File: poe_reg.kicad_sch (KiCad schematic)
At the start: 21 parts, among them U3 MP6004GQ-P

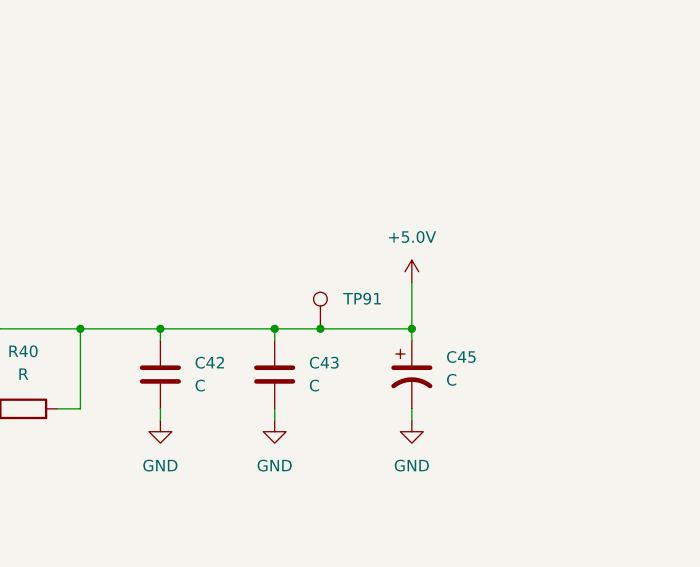
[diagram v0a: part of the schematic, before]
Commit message: did 3v3 reg
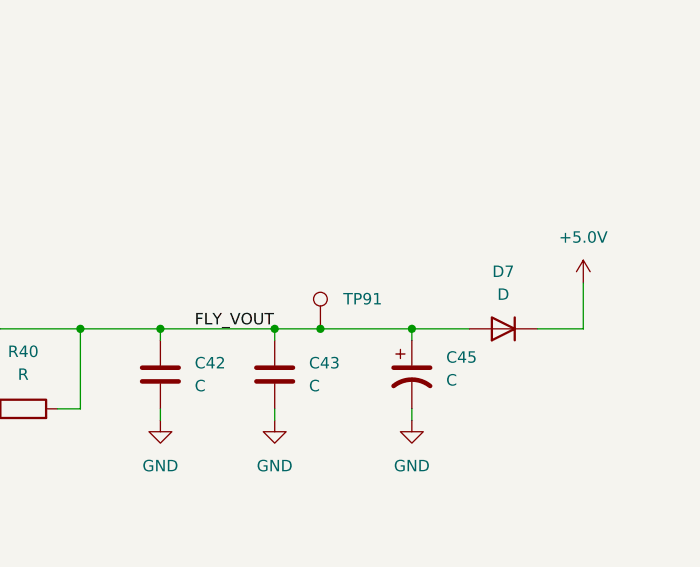
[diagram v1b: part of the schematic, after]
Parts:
- added D7: D, symbol Device:D
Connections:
- net +5.0V: now also D7.1 (K); no longer C42.1, C43.1, C45.1, D6.1 (K), R40.2, TP91.1
- new net FLY_VOUT: C42.1, C43.1, C45.1, D6.1 (K), D7.2 (A), R40.2, TP91.1
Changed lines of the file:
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@@
+	)
+	(junction
+		(at 250.19 88.9)
+		(diameter 0)
+		(color 0 0 0 0)
 	)
 	(junction
@@
 	)
 	(junction
-		(at 250.19 88.9)
-		(diameter 0)
-		(color 0 0 0 0)
-	)
-	(junction
 		(at 139.7 67.31)
 		(diameter 0)
@@
 	(wire
 		(pts
+			(xy 264.16 88.9) (xy 269.24 88.9)
+		)
+		(stroke
+			(width 0)
+			(type default)
+		)
+	)
+	(wire
+		(pts
 			(xy 149.86 77.47) (xy 139.7 77.47)
 		)
@@
 	(wire
 		(pts
-			(xy 250.19 83.82) (xy 250.19 88.9)
-		)
-		(stroke
-			(width 0)
-			(type default)
-		)
-	)
-	(wire
-		(pts
 			(xy 149.86 77.47) (xy 149.86 78.74)
 		)
@@
 	(wire
 		(pts
+			(xy 250.19 88.9) (xy 256.54 88.9)
+		)
+		(stroke
+			(width 0)
+			(type default)
+		)
+	)
+	(wire
+		(pts
 			(xy 250.19 97.79) (xy 250.19 99.06)
 		)
@@
 		(pts
 			(xy 86.36 92.71) (xy 92.71 92.71)
+		)
+		(stroke
+			(width 0)
+			(type default)
+		)
+	)
+	(wire
+		(pts
+			(xy 269.24 83.82) (xy 269.24 88.9)
 		)
 		(stroke
@@
 	(label "FLY_SW"
 		(at 135.89 93.98 0)
+		(effects
+			(font
+				(size 1.27 1.27)
+			)
+			(justify left bottom)
+		)
+	)
+	(label "FLY_VOUT"
+		(at 226.06 88.9 0)
 		(effects
 			(font
@@
 	)
 	(symbol
+		(lib_id "Device:D")
+		(at 260.35 88.9 180)
+		(unit 1)
+		(exclude_from_sim no)
+		(in_bom yes)
+		(on_board yes)
+		(dnp no)
+		(fields_autoplaced yes)
+		(property "Reference" "D7"
+			(at 260.35 82.55 0)
+			(effects
+				(font
+					(size 1.27 1.27)
+				)
+			)
+		)
+		(property "Value" "D"
+			(at 260.35 85.09 0)
+			(effects
+				(font
+					(size 1.27 1.27)
+				)
+			)
+		)
+		(property "Footprint" ""
+			(at 260.35 88.9 0)
+			(effects
+				(font
+					(size 1.27 1.27)
+				)
+				(hide yes)
+			)
+		)
+		(property "Datasheet" "~"
+			(at 260.35 88.9 0)
+			(effects
+				(font
+					(size 1.27 1.27)
+				)
+				(hide yes)
+			)
+		)
+		(property "Description" "Diode"
+			(at 260.35 88.9 0)
+			(effects
+				(font
+					(size 1.27 1.27)
+				)
+				(hide yes)
+			)
+		)
+		(property "Sim.Device" "D"
+			(at 260.35 88.9 0)
+			(effects
+				(font
+					(size 1.27 1.27)
+				)
+				(hide yes)
+			)
+		)
+		(property "Sim.Pins" "1=K 2=A"
+			(at 260.35 88.9 0)
+			(effects
+				(font
+					(size 1.27 1.27)
+				)
+				(hide yes)
+			)
+		)
+		(pin "2"
+		)
+		(pin "1"
+		)
+		(instances
+			(project ""
+				(path "/2970f661-65ab-4e2b-aeda-d76d1044f2b8/475d46f3-a9d1-4d0e-882c-449f9a11ef3e"
+					(reference "D7")
+					(unit 1)
+				)
+			)
+		)
+	)
+	(symbol
 		(lib_id "Connector:TestPoint_Alt")
 		(at 154.94 135.89 0)
@@
 	(symbol
 		(lib_id "power:+3.3V")
-		(at 250.19 83.82 0)
+		(at 269.24 83.82 0)
 		(unit 1)
 		(exclude_from_sim no)
@@
 		(fields_autoplaced yes)
 		(property "Reference" "#PWR074"
-			(at 250.19 87.63 0)
+			(at 269.24 87.63 0)
 			(effects
 				(font
@@
 		)
 		(property "Value" "+5.0V"
-			(at 250.19 78.74 0)
+			(at 269.24 78.74 0)
 			(effects
 				(font
@@
 		)
 		(property "Footprint" ""
-			(at 250.19 83.82 0)
+			(at 269.24 83.82 0)
 			(effects
 				(font
@@
 		)
 		(property "Datasheet" ""
-			(at 250.19 83.82 0)
+			(at 269.24 83.82 0)
 			(effects
 				(font
@@
 		)
 		(property "Description" "Power symbol creates a global label with name \"+3.3V\""
-			(at 250.19 83.82 0)
-			(effects
-				(font
-					(size 1.27 1.27)
-				)
-				(hide yes)
-			)
-		)
-		(pin "1"
-		)
-		(instances
-			(project ""
+			(at 269.24 83.82 0)
+			(effects
+				(font
+					(size 1.27 1.27)
+				)
+				(hide yes)
+			)
+		)
+		(pin "1"
+		)
+		(instances
+			(project "netdaq"
 				(path "/2970f661-65ab-4e2b-aeda-d76d1044f2b8/475d46f3-a9d1-4d0e-882c-449f9a11ef3e"
 					(reference "#PWR074")

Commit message: did stuff
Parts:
- renumbered C38 to C102, C42 to C103, C43 to C104, C45 to C105, C40 to C106, C39 to C107, C41 to C108, D5 to D37, D6 to D38, D7 to D39, R37 to R76, R40 to R77, R38 to R78, R39 to R79, TP93 to TP122, TP90 to TP123, TP91 to TP124, TP92 to TP125, TP94 to TP126, TP95 to TP127, U3 to U5

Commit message: lots
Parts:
- removed D39: D, symbol Device:D
- removed TR2: Wuerth_750343373, Transformer_THT:Transformer_Wuerth_750343373, symbol Transformer:Wuerth_750343373
- added C134: 47u, Capacitor_SMD:C_Elec_10x10.2, symbol Device:C_Polarized_US
- added D80: MMBZ5256ELT1G, MMBZ5256ELT1G:SOT-23(1-3), symbol Device:D_Zener
- added R103: 500, Resistor_SMD:R_0603_1608Metric, symbol Device:R
- added R104: 13k, Resistor_SMD:R_0402_1005Metric, symbol Device:R
- added R105: 10k, Resistor_SMD:R_0402_1005Metric, symbol Device:R
- added R106: 330k, Resistor_SMD:R_0402_1005Metric, symbol Device:R
- added T2: POE30P-50L, POE30P-50L:POE30P-50L, symbol POE30P-50L:POE30P-50L
- C102: value C -> 910p; footprint (none) -> Capacitor_SMD:C_0402_1005Metric
- C103, C104: value C -> 22u 10 V; footprint (none) -> Capacitor_SMD:C_0805_2012Metric
- C105: value C -> 220u; footprint (none) -> Capacitor_SMD:C_Elec_6.3x7.7
- C106: value C -> 2.2u 100 V; footprint (none) -> Capacitor_SMD:C_1206_3216Metric
- C107: value C -> 1u 10V; footprint (none) -> Capacitor_SMD:C_0402_1005Metric
- C108: footprint (none) -> Capacitor_SMD:C_0402_1005Metric; now not fitted
- D37: value D -> US1MFA; footprint (none) -> Diode_SMD:D_SOD-123F
- D38: value D -> VS-10BQ060-M3/5BT; footprint (none) -> SMB:SMB(DO-214AA); symbol Device:D -> Device:D_Schottky
- R76: value R -> 56k; footprint (none) -> Resistor_SMD:R_0402_1005Metric
- R77: footprint (none) -> Resistor_SMD:R_0402_1005Metric; now not fitted
- R78: value R -> 68k; footprint (none) -> Resistor_SMD:R_0402_1005Metric
- R79: value R -> 12k; footprint (none) -> Resistor_SMD:R_0402_1005Metric
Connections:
- net ETH_SHIELD is gone; now on net PGND: C106.2, C107.2, R79.2, TP126.1, U5.1 (GND), U5.10 (AGND), U5.15 (EPAD), U5.2 (GND)
- net FLY_VOUT is gone; now on net +5.0V: C103.1, C104.1, C105.1, D38.1 (K), R77.2, TP124.1
- net +5.0V: now also R103.2
- net FLY_CT: now also T2.2
- net FLY_SW: now also T2.3
- net GND: now also R103.1, T2.7, T2.8
- net VIN: now also C134.1, D80.1 (K), T2.4
- net at C108.1, D38.2 (A), TP123.1: now also T2.5, T2.6
- net FLY_EN: now reaches U5.3 (EN)
- net FLY_EN: now also R104.1, R105.2
- net PGND: now reaches U5.7 (MODE)
- net PGND: now also C134.2, R104.2, R106.2, T2.1
- net at U5.9 (ILIM): now also R106.1
- new net: D80.2 (A), R105.1
- no-connect marks 0 -> 1
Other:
- moved on the sheet: C102, C103, C104, C105, C107, D37, D38, R76, R78, R79, TP122, TP123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

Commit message: changed to 4 layer, finished usb conn, added jtag conn, some other things
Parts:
- TP122, TP123, TP124, TP125: footprint (none) -> TestPoint:TestPoint_THTPad_D1.0mm_Drill0.5mm
- TP126, TP127: footprint (none) -> TestPoint:TestPoint_THTPad_1.0x1.0mm_Drill0.5mm
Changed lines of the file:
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@@
 			)
 		)
-		(property "Footprint" ""
+		(property "Footprint" "TestPoint:TestPoint_THTPad_D1.0mm_Drill0.5mm"
 			(at 228.6 124.46 0)
 			(hide yes)
@@
 			)
 		)
-		(property "Footprint" ""
+		(property "Footprint" "TestPoint:TestPoint_THTPad_1.0x1.0mm_Drill0.5mm"
 			(at 198.12 207.01 0)
 			(hide yes)
@@
 			)
 		)
-		(property "Footprint" ""
+		(property "Footprint" "TestPoint:TestPoint_THTPad_D1.0mm_Drill0.5mm"
 			(at 191.77 109.22 0)
 			(hide yes)
@@
 			)
 		)
-		(property "Footprint" ""
+		(property "Footprint" "TestPoint:TestPoint_THTPad_D1.0mm_Drill0.5mm"
 			(at 191.77 135.89 0)
 			(hide yes)
@@
 			)
 		)
-		(property "Footprint" ""
+		(property "Footprint" "TestPoint:TestPoint_THTPad_D1.0mm_Drill0.5mm"
 			(at 283.21 124.46 0)
 			(hide yes)
@@
 			)
 		)
-		(property "Footprint" ""
+		(property "Footprint" "TestPoint:TestPoint_THTPad_1.0x1.0mm_Drill0.5mm"
 			(at 232.41 177.8 0)
 			(hide yes)

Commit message: many stuffs
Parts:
- added TP180: TestPoint, TestPoint:TestPoint_THTPad_D1.0mm_Drill0.5mm, symbol Connector:TestPoint
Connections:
- net FLY_EN: now also TP180.1
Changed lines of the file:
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@@
+	)
+	(junction
+		(at 105.41 149.86)
+		(diameter 0)
+		(color 0 0 0 0)
 	)
 	(junction
@@
 	(wire
 		(pts
+			(xy 105.41 148.59) (xy 105.41 149.86)
+		)
+		(stroke
+			(width 0)
+			(type default)
+		)
+	)
+	(wire
+		(pts
 			(xy 109.22 109.22) (xy 124.46 109.22)
 		)
@@
 	(wire
 		(pts
-			(xy 96.52 149.86) (xy 133.35 149.86)
+			(xy 96.52 149.86) (xy 105.41 149.86)
 		)
 		(stroke
@@
 		(pts
 			(xy 118.11 143.51) (xy 118.11 144.78)
+		)
+		(stroke
+			(width 0)
+			(type default)
+		)
+	)
+	(wire
+		(pts
+			(xy 105.41 149.86) (xy 133.35 149.86)
 		)
 		(stroke
@@
 					(unit 1)
 				)
+			)
+		)
+	)
+	(symbol
+		(lib_id "Connector:TestPoint")
+		(at 105.41 148.59 0)
+		(mirror y)
+		(unit 1)
+		(body_style 1)
+		(exclude_from_sim no)
+		(in_bom yes)
+		(on_board yes)
+		(in_pos_files yes)
+		(dnp no)
+		(fields_autoplaced yes)
+		(property "Reference" "TP180"
+			(at 107.95 145.2879 0)
+			(show_name no)
+			(do_not_autoplace no)
+			(effects
+				(font
+					(size 1.27 1.27)
+				)
+				(justify right)
+			)
+		)
+		(property "Value" "TestPoint"
+			(at 104.1401 143.51 90)
+			(hide yes)
+			(show_name no)
+			(do_not_autoplace no)
+			(effects
+				(font
+					(size 1.27 1.27)
+				)
+				(justify left)
+			)
+		)
+		(property "Footprint" "TestPoint:TestPoint_THTPad_D1.0mm_Drill0.5mm"
+			(at 100.33 148.59 0)
+			(hide yes)
+			(show_name no)
+			(do_not_autoplace no)
+			(effects
+				(font
+					(size 1.27 1.27)
+				)
+			)
+		)
+		(property "Datasheet" ""
+			(at 100.33 148.59 0)
+			(hide yes)
+			(show_name no)
+			(do_not_autoplace no)
+			(effects
+				(font
+					(size 1.27 1.27)
+				)
+			)
+		)
+		(property "Description" "test point"
+			(at 105.41 148.59 0)
+			(hide yes)
+			(show_name no)
+			(do_not_autoplace no)
+			(effects
+				(font
+					(size 1.27 1.27)
+				)
+			)
+		)
+		(pin "1"
+		)
+		(instances
+			(project "netdaq"
+				(path "/2970f661-65ab-4e2b-aeda-d76d1044f2b8/475d46f3-a9d1-4d0e-882c-449f9a11ef3e"
+					(reference "TP180")
+					(unit 1)
+				)

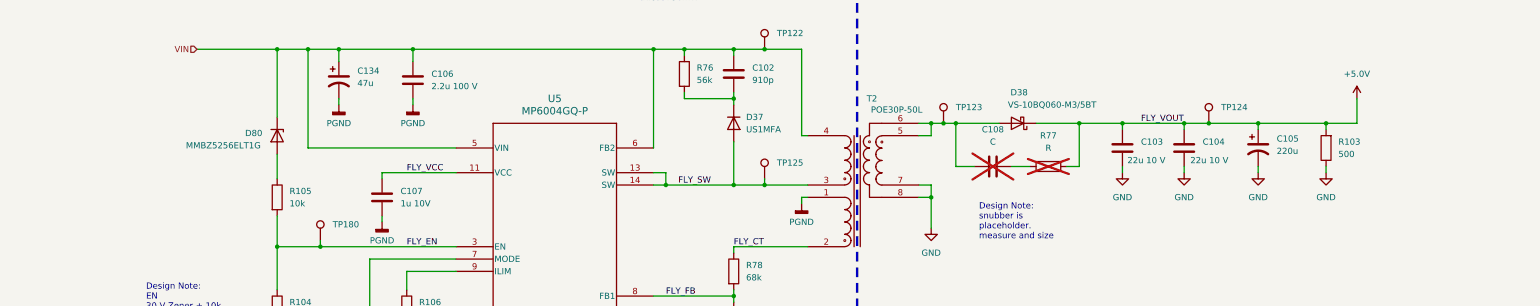
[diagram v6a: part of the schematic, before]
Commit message: did a bunch of bom matching to lcsc
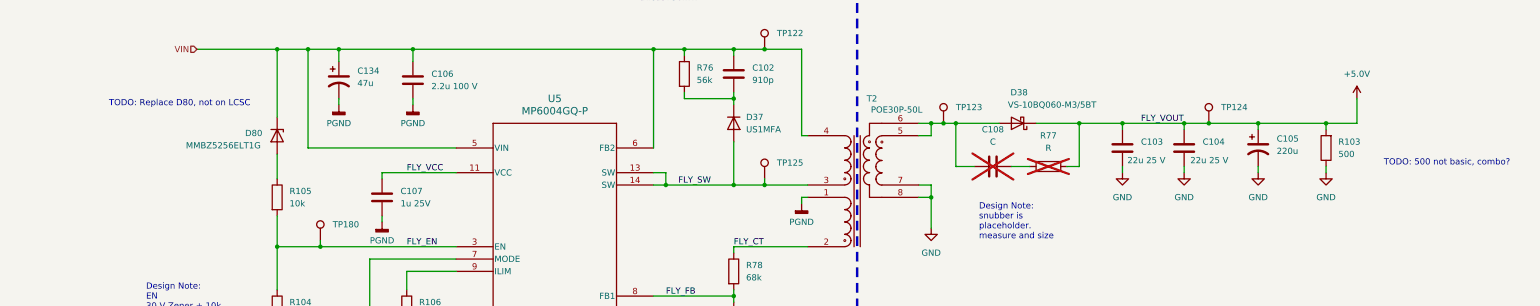
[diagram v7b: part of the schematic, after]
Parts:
- C102, C105, C134, R103: LCSC Basic/Pref (none) -> n
- C103, C104: value 22u 10 V -> 22u 25 V; LCSC (none) -> C45783; LCSC Basic/Pref (none) -> x; LCSC Part (none) -> C45783
- C107: value 1u 10V -> 1u 25V; LCSC (none) -> C52923; LCSC Basic/Pref (none) -> x; LCSC Part (none) -> C52923
- D37: LCSC Part (none) -> C894760
- D38: LCSC (none) -> C469520; LCSC Part (none) -> C469520
- D80, T2, U5: LCSC missing (none) -> x
- R104: footprint Resistor_SMD:R_0402_1005Metric -> Resistor_SMD:R_0603_1608Metric; LCSC (none) -> C22797; LCSC Basic/Pref (none) -> x; LCSC Part (none) -> C22797
- R105: LCSC (none) -> C25744; LCSC Basic/Pref (none) -> x; LCSC Part (none) -> C25744
- R106: LCSC (none) -> C25778; LCSC Basic/Pref (none) -> x; LCSC Part (none) -> C25778
- R76: LCSC (none) -> C25796; LCSC Basic/Pref (none) -> x; LCSC Part (none) -> C25796
- R78: LCSC (none) -> C36871; LCSC Basic/Pref (none) -> x; LCSC Part (none) -> C36871
- R79: LCSC (none) -> C25752; LCSC Basic/Pref (none) -> x; LCSC Part (none) -> C25752
- TP122, TP123, TP124, TP125, TP126, TP127, TP180: now left out of the parts list
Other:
- note added: "TODO: 500 not basic, combo?"
- note added: "TODO: Replace D80, not on LCSC"

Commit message: did almost nothing!
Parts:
- added R107: 200, Resistor_SMD:R_0603_1608Metric, symbol Device:R
- R103: value 500 -> 300; LCSC (none) -> C25102; LCSC Basic/Pref n -> y; LCSC Part (none) -> C25102
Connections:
- net GND: now also R107.1; no longer R103.1
- net +5.0V renamed +5.2V
- new net: R103.1, R107.2
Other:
- note added: "TODO: recalc for 5.2 V"
- note removed: "TODO: 500 not basic, combo?"
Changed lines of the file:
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@@
 	(generator_version "10.0")
 	(paper "A3")
-	(text "TODO: 500 not basic, combo?"
+	(text "TODO: recalc for 5.2 V"
 		(exclude_from_sim no)
-		(at 337.312 132.588 0)
+		(at 133.858 98.806 0)
 		(effects
 			(font
@@
 	(wire
 		(pts
+			(xy 312.42 133.35) (xy 312.42 135.89)
+		)
+		(stroke
+			(width 0)
+			(type default)
+		)
+	)
+	(wire
+		(pts
 			(xy 132.08 180.34) (xy 133.35 180.34)
 		)
@@
 	(wire
 		(pts
+			(xy 312.42 143.51) (xy 312.42 146.05)
+		)
+		(stroke
+			(width 0)
+			(type default)
+		)
+	)
+	(wire
+		(pts
 			(xy 173.99 134.62) (xy 176.53 134.62)
 		)
@@
 	(wire
 		(pts
-			(xy 312.42 133.35) (xy 312.42 134.62)
-		)
-		(stroke
-			(width 0)
-			(type default)
-		)
-	)
-	(wire
-		(pts
 			(xy 228.6 127) (xy 231.14 127)
 		)
@@
 	)
 	(symbol
+		(lib_id "Device:R")
+		(at 312.42 139.7 180)
+		(unit 1)
+		(body_style 1)
+		(exclude_from_sim no)
+		(in_bom yes)
+		(on_board yes)
+		(in_pos_files yes)
+		(dnp no)
+		(fields_autoplaced yes)
+		(property "Reference" "R107"
+			(at 314.96 138.4299 0)
+			(show_name no)
+			(do_not_autoplace no)
+			(effects
+				(font
+					(size 1.27 1.27)
+				)
+				(justify right)
+			)
+		)
+		(property "Value" "200"
+			(at 314.96 140.9699 0)
+			(show_name no)
+			(do_not_autoplace no)
+			(effects
+				(font
+					(size 1.27 1.27)
+				)
+				(justify right)
+			)
+		)
+		(property "Footprint" "Resistor_SMD:R_0603_1608Metric"
+			(at 314.198 139.7 90)
+			(hide yes)
+			(show_name no)
+			(do_not_autoplace no)
+			(effects
+				(font
+					(size 1.27 1.27)
+				)
+			)
+		)
+		(property "Datasheet" ""
+			(at 312.42 139.7 0)
+			(hide yes)
+			(show_name no)
+			(do_not_autoplace no)
+			(effects
+				(font
+					(size 1.27 1.27)
+				)
+			)
+		)
+		(property "Description" "Resistor"
+			(at 312.42 139.7 0)
+			(hide yes)
+			(show_name no)
+			(do_not_autoplace no)
+			(effects
+				(font
+					(size 1.27 1.27)
+				)
+			)
+		)
+		(property "Sim.Type" ""
+			(at 312.42 139.7 0)
+			(hide yes)
+			(show_name no)
+			(do_not_autoplace no)
+			(effects
+				(font
+					(size 1.27 1.27)
+				)
+			)
+		)
+		(property "KLC_S3.3" ""
+			(at 312.42 139.7 0)
+			(hide yes)
+			(show_name no)
+			(do_not_autoplace no)
+			(effects
+				(font
+					(size 1.27 1.27)
+				)
+			)
+		)
+		(property "KLC_S4.1" ""
+			(at 312.42 139.7 0)
+			(hide yes)
+			(show_name no)
+			(do_not_autoplace no)
+			(effects
+				(font
+					(size 1.27 1.27)
+				)
+			)
+		)
+		(property "LCSC Basic/Pref" "y"
+			(at 312.42 139.7 0)
+			(hide yes)
+			(show_name no)
+			(do_not_autoplace no)
+			(effects
+				(font
+					(size 1.27 1.27)
+				)
+			)
+		)
+		(property "LCSC missing" ""
+			(at 312.42 139.7 0)
+			(hide yes)
+			(show_name no)
+			(do_not_autoplace no)
+			(effects
+				(font
+					(size 1.27 1.27)
+				)
+			)
+		)
+		(property "LCSC" "C25087"
+			(at 312.42 139.7 0)
+			(hide yes)
+			(show_name no)
+			(do_not_autoplace no)
+			(effects
+				(font
+					(size 1.27 1.27)
+				)
+			)
+		)
+		(property "LCSC Part" "C25087"
+			(at 312.42 139.7 0)
+			(hide yes)
+			(show_name no)
+			(do_not_autoplace no)
+			(effects
+				(font
+					(size 1.27 1.27)
+				)
+			)
+		)
+		(pin "1"
+		)
+		(pin "2"
+		)
+		(instances
+			(project "netdaq"
+				(path "/2970f661-65ab-4e2b-aeda-d76d1044f2b8/475d46f3-a9d1-4d0e-882c-449f9a11ef3e"
+					(reference "R107")
+					(unit 1)
+				)
+			)
+		)
+	)
+	(symbol
 		(lib_id "Device:D_Schottky")
 		(at 248.92 124.46 180)
@@
 			)
 		)
-		(property "Value" "500"
+		(property "Value" "300"
 			(at 314.96 130.8099 0)
 			(show_name no)
@@
 			)
 		)
-		(property "LCSC Basic/Pref" "n"
+		(property "LCSC Basic/Pref" "y"
 			(at 312.42 129.54 0)
 			(hide yes)
@@
 			)
 		)
-		(pin "1"
-		)
-		(pin "2"
-		)
-		(instances
-			(project "netdaq"
-				(path "/2970f661-65ab-4e2b-aeda-d76d1044f2b8/475d46f3-a9d1-4d0e-882c-449f9a11ef3e"
-					(reference "R103")
-					(unit 1)
-				)
-			)
-		)
-	)
-	(symbol
-		(lib_id "power:GND")
-		(at 312.42 134.62 0)
-		(unit 1)
-		(body_style 1)
-		(exclude_from_sim no)
-		(in_bom yes)
-		(on_board yes)
-		(in_pos_files yes)
-		(dnp no)
-		(fields_autoplaced yes)
-		(property "Reference" "#PWR0169"
-			(at 312.42 140.97 0)
-			(hide yes)
-			(show_name no)
-			(do_not_autoplace no)
-			(effects
-				(font
-					(size 1.27 1.27)
-				)
-			)
-		)
-		(property "Value" "GND"
-			(at 312.42 139.7 0)
-			(show_name no)
-			(do_not_autoplace no)
-			(effects
-				(font
-					(size 1.27 1.27)
-				)
-			)
-		)
-		(property "Footprint" ""
-			(at 312.42 134.62 0)
-			(hide yes)
-			(show_name no)
-			(do_not_autoplace no)
-			(effects
-				(font
-					(size 1.27 1.27)
-				)
-			)
-		)
-		(property "Datasheet" ""
-			(at 312.42 134.62 0)
+		(property "LCSC" "C25102"
+			(at 312.42 129.54 0)
 			(hide yes)
 			(show_name no)
@@
 			)
 		)
-		(property "Description" "Power symbol creates a global label with name \"GND\" , ground"
-			(at 312.42 134.62 0)
+		(property "LCSC Part" "C25102"
+			(at 312.42 129.54 0)
 			(hide yes)
 			(show_name no)
@@
 		(pin "1"
 		)
+		(pin "2"
+		)
 		(instances
 			(project "netdaq"
 				(path "/2970f661-65ab-4e2b-aeda-d76d1044f2b8/475d46f3-a9d1-4d0e-882c-449f9a11ef3e"
-					(reference "#PWR0169")
+					(reference "R103")
 					(unit 1)
 				)
@@
 	)
 	(symbol
+		(lib_id "power:GND")
+		(at 312.42 146.05 0)
+		(unit 1)
+		(body_style 1)
+		(exclude_from_sim no)
+		(in_bom yes)
+		(on_board yes)
+		(in_pos_files yes)
+		(dnp no)
+		(fields_autoplaced yes)
+		(property "Reference" "#PWR0169"
+			(at 312.42 152.4 0)
+			(hide yes)
+			(show_name no)
+			(do_not_autoplace no)
+			(effects
+				(font
+					(size 1.27 1.27)
+				)
+			)
+		)
+		(property "Value" "GND"
+			(at 312.42 151.13 0)
+			(show_name no)
+			(do_not_autoplace no)
+			(effects
+				(font
+					(size 1.27 1.27)
+				)
+			)
+		)
+		(property "Footprint" ""
+			(at 312.42 146.05 0)
+			(hide yes)
+			(show_name no)
+			(do_not_autoplace no)
+			(effects
+				(font
+					(size 1.27 1.27)
+				)
+			)
+		)
+		(property "Datasheet" ""
+			(at 312.42 146.05 0)
+			(hide yes)
+			(show_name no)
+			(do_not_autoplace no)
+			(effects
+				(font
+					(size 1.27 1.27)
+				)
+			)
+		)
+		(property "Description" "Power symbol creates a global label with name \"GND\" , ground"
+			(at 312.42 146.05 0)
+			(hide yes)
+			(show_name no)
+			(do_not_autoplace no)
+			(effects
+				(font
+					(size 1.27 1.27)
+				)
+			)
+		)
+		(pin "1"
+		)
+		(instances
+			(project "netdaq"
+				(path "/2970f661-65ab-4e2b-aeda-d76d1044f2b8/475d46f3-a9d1-4d0e-882c-449f9a11ef3e"
+					(reference "#PWR0169")
+					(unit 1)
+				)
+			)
+		)
+	)
+	(symbol
 		(lib_id "Device:R")
 		(at 180.34 114.3 0)
@@
 			)
 		)
-		(property "Value" "+5.0V"
-			(at 318.77 114.3 0)
+		(property "Value" "+5.2V"
+			(at 321.31 118.1099 0)
 			(show_name no)
 			(do_not_autoplace no)
@@
 					(size 1.27 1.27)
 				)
+				(justify left)
 			)
 		)
